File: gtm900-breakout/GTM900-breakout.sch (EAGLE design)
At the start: 43 parts, among them K1 694108106102, T1 BC847, U1 FH12A-40S-0.5SH(55), U2 FH12A-40S-0.5SH(55), U3 MCP1827T-ADJE/ET

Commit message: gtm900: added CP2105 and 3.5mm TRRS audio jack, remv'd aux conn
adds to OS#4030
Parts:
- removed JP2: (no value), jumper:JP1E
- added C15, C19: 4.7u, rc-sysmocom:CAP_CERAMIC_0603
- added C16: 1u, rc-sysmocom:CAP_CERAMIC_0603
- added C17, C18, C20, C27, C28: 100n, rc-sysmocom:CAP_CERAMIC_0603
- added C21, C22, C23, C24, C25, C26, C30, C31, C32: 33p, rc-sysmocom:CAP_CERAMIC_0402
- added C29: 22u, rc-sysmocom:CAP_CERAMIC_0603
- added J1: SJ2-3574A, SparkFun-Connectors:AUDIO-JACK3
- added K2: 615004143821, Wuerth_Elektronik_eiCan_Communication_Connectors_v6_20150113:615004143821
- added R12: 4.7k, rc-sysmocom:RESISTOR_0603
- added R13: 1M, rc-sysmocom:RESISTOR_0603
- added R14, R17: 100, rc-sysmocom:RESISTOR_0402
- added R15, R16: 2.2k, rc-sysmocom:RESISTOR_0402
- added U4: CP2105-GM, usb-uart:CP2105-GM
- added U5: IP4234CZ6, laforge:IP4234CZ6
- added X3: MINI-USB-SHIELD-UX60-MB-5ST, con-hirose:MINI-USB-SHIELD-UX60-MB-5ST
- B1, MDM1: CLASS (none) -> UNKNOWN CLASS; DESCRIPTION (none) -> NO DESCRIPTION; LINK (none) -> UNKNOWN LINK; MANUFACTURER (none) -> UNKNOWN MANUFACTURER; MANUFACTURERPARTNUMBER (none) -> UNKNOWN MANUFACTURER PART NUMBER; POPULATED (none) -> TRUE; ROHSCERTIFICATE (none) -> UNKNOWN ROHS CERTIFICATE; SOURCE (none) -> UNKNOWN SOURCE; SOURCEPARTNUMBER (none) -> UNKNOWN SOURCE PART NUMBER
- JP1: device laforge:PINHD-2X10 -> jumper:JP1E
- R11: value 22k -> 15k; DESCRIPTION RES 22K OHM 1/10W 1% 0603 SMD -> RES SMD 15K OHM 1%% 1/10W 0603; LINK http://www.digikey.de/product-detail/de/MCR03ERTF2202/RHM22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 -> https://www.digikey.de/product-detail/de/yageo/RC0603FR-071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; MANUFACTURER Rohm Semiconductor -> Yageo; MANUFACTURERPARTNUMBER MCR03ERTF2202 -> RC0603FR-0715KL; ROHSCERTIFICATE Bleifrei / RoHS-konform -> UNKNOWN ROHS CERTIFICATE; SOURCEPARTNUMBER RHM22.0KCFCT-ND -> 311-15.0KHRCT-ND
- R6: value 200k -> 22k; DESCRIPTION RES 200K OHM 1/16W 1% 0603 -> RES 22K OHM 1/10W 1% 0603 SMD; LINK http://www.digikey.de/product-detail/de/8-1879338-5/A102235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 -> http://www.digikey.de/product-detail/de/MCR03ERTF2202/RHM22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; MANUFACTURER TE Connectivity -> Rohm Semiconductor; MANUFACTURERPARTNUMBER 8-1879338-5 -> MCR03ERTF2202; SOURCEPARTNUMBER A102235CT-ND -> RHM22.0KCFCT-ND
- R8: value 15k -> 330; DESCRIPTION RES SMD 15K OHM 1%% 1/10W 0603 -> RES SMD 330 OHM 5% 1/10W 0603; LINK https://www.digikey.de/product-detail/de/yageo/RC0603FR-071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 -> http://www.digikey.com/product-detail/en/yageo/RC0603JR-073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; MANUFACTURERPARTNUMBER RC0603FR-0715KL -> RC0603JR-07330RL; SOURCEPARTNUMBER 311-15.0KHRCT-ND -> 311-330GRCT-ND
- R9: value 330 -> 200k; DESCRIPTION RES SMD 330 OHM 5% 1/10W 0603 -> RES 200K OHM 1/16W 1% 0603; LINK http://www.digikey.com/product-detail/en/yageo/RC0603JR-073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 -> http://www.digikey.de/product-detail/de/8-1879338-5/A102235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; MANUFACTURER Yageo -> TE Connectivity; MANUFACTURERPARTNUMBER RC0603JR-07330RL -> 8-1879338-5; ROHSCERTIFICATE UNKNOWN ROHS CERTIFICATE -> Bleifrei / RoHS-konform; SOURCEPARTNUMBER 311-330GRCT-ND -> A102235CT-ND
- U1, U2: CLASS (none) -> IC; DESCRIPTION (none) -> NO DESCRIPTION; LINK (none) -> UNKNOWN LINK; MANUFACTURER (none) -> UNKNOWN MANUFACTURER; MANUFACTURERPARTNUMBER (none) -> UNKNOWN MANUFACTURER PART NUMBER; POPULATED (none) -> TRUE; ROHSCERTIFICATE (none) -> UNKNOWN ROHS CERTIFICATE; SOURCE (none) -> UNKNOWN SOURCE; SOURCEPARTNUMBER (none) -> UNKNOWN SOURCE PART NUMBER
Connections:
- removed net N$24: JP1.12
- new net N$11: C20.2, R13.2, X3S.S1, X3S.S2, X3S.S3, X3S.S4
- new net N$12: R12.1, U4.!RST
- new net N$14: C15.2, U4.NC/DCD_ECI
- new net N$15: C27.2, C31.1, J1.RING2, R15.2
- new net N$16: C29.1, C30.1, R14.2, R15.1
- new net N$17: C29.2, C30.2, R16.2, R17.1
- new net N$20: C28.2, C31.2, J1.TIP, R16.1
- new net USB_DN: U4.D_MINUS, U5.2B
- new net USB_DP: U4.D_PLUS, U5.1B
- new net USB_VBUS: C16.1, U4.REGIN, U4.VBUS, U5.VCC, X3G$1.1
- new net VDD_3V45: C18.1, C19.1, U4.VDD
- new net _USB_DN: U5.2A, X3G$1.2
- new net _USB_DP: U5.1A, X3G$1.3
- net !RST: now also R11.2; no longer R8.2
- net ADC: no longer JP1.2
- net AUXI+: no longer JP1.19
- net AUXI-: no longer JP1.20
- net AUXO+: no longer JP1.13
- net AUXO-: no longer JP1.14
- net EAR+: now also C23.1, C26.1, C32.2, J1.RING1; no longer JP1.15
- net EAR-: now also C24.2, C26.2, C32.1, J1.EARTH; no longer JP1.16
- net GND: now also C15.1, C16.2, C17.1, C18.2, C19.2, C20.1, C21.2, C22.1, C23.2, C24.1, JP1.2, R13.1, R17.2, U4.GND, U4.HEAT_TAB, U5.GND, X3G$1.5; no longer JP1.3, JP2.2
- net LPG: now also R6.1; no longer R11.1
- net MIC+: now also C21.1, C25.1, C27.1; no longer JP1.17
- net MIC-: now also C22.2, C25.2, C28.1; no longer JP1.18
- net N$2: now also R8.2; no longer R9.2
- net N$5: now also R6.2, R7.1; no longer R10.1, R11.2
- net N$6: now also R10.1, R9.1; no longer R6.1, R7.1
- net PWON: now also JP1.1; no longer JP2.1
- net RXD2: now also U4.RXD_ECI
- net TXD2: now also U4.TXD_ECI
- net UART_CTS: now also U4.CTS_SCI; no longer JP1.8
- net UART_DCD: now also U4.GPIO.0_SCI/DCD_SCI; no longer JP1.11
- net UART_DSR: now also U4.GPIO.2_SCI/DSR_SCI; no longer JP1.4
- net UART_DTR: now also U4.GPIO.1_SCI/DTR_SCI; no longer JP1.10
- net UART_RI: now also U4.!SUSPEND/RI_SCI; no longer JP1.5
- net UART_RTS: now also U4.RTS_SCI; no longer JP1.9
- net UART_RXD: now also U4.RXD_SCI; no longer JP1.6
- net UART_TXD: now also U4.TXD_SCI; no longer JP1.7
- net VCC: now also R11.1, R9.2; no longer JP1.1, R6.2, R9.1
- net VDD: now also C17.2, R12.2, R14.1, U4.VIO
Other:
- note added: "audio i/o (1st channel)"
- note added: "dual USB UART"
- note added: "for programming"
- note removed: "AUX socket / I/O Header"

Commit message: gtm900-bo: hopefully incorporating all we discussed last weeks
see OS#4030
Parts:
- removed K2: 615004143821, Wuerth_Elektronik_eiCan_Communication_Connectors_v6_20150113:615004143821
- added B2: (no value), microbuilder:SWITCH_TACT_SMT
- added C33, C34: 33p, rc-sysmocom:CAP_CERAMIC_0402
- added D5: PESD5V0UBV, laforge:PESD5V0UBV
- added JP2: (no value), microbuilder:HEADER-1X476MIL
- added R18, R20, R21: 22k, rc-sysmocom:RESISTOR_0603
- added R19: 330, rc-sysmocom:RESISTOR_0603
- added R22: DNP, rc-sysmocom:RESISTOR_0603
- added R23: 1k, rc-sysmocom:RESISTOR_0603
- added R24: 4.7k, rc-sysmocom:RESISTOR_0603
- added R25: 1M, rc-sysmocom:RESISTOR_0603
- added R26: 0, rc-sysmocom:RESISTOR_0603
- added T2, T3, T4: BC847, transistor:BC847C-NPN-SOT23-BEC
- added TP1, TP2, TP3, TP4, TP5: TPTP10R, testpad:TPTP10R
- added U6: IP4234CZ6, laforge:IP4234CZ6
- added X4: MINI-USB-SHIELD-UX60-MB-5ST, con-hirose:MINI-USB-SHIELD-UX60-MB-5ST
- C10: value 470u -> 100u; device rcl:CPOL-EUUD-8X10 -> rc-sysmocom:CAP_CERAMIC1206; DESCRIPTION 470µF 6.3V Aluminum Capacitors Radial, Can - SMD 2000 Hrs @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 -> 100µF 6.3V Ceramic Capacitor X5R 1206 (3216 Metric) 0.126" 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; LINK http://www.digikey.com/product-detail/en/nichicon/UUR0J471M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 -> http://www.digikey.com/product-detail/en/murata-electronics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; MANUFACTURER Nichicon -> Murata Electronics North America; MANUFACTURERPARTNUMBER UUR0J471MNL1GS -> GRM31CR60J107ME39K; SOURCEPARTNUMBER 493-6207-1-ND -> 490-7217-1-ND
- C11: value 100u -> 470u; device rc-sysmocom:CAP_CERAMIC1206 -> rcl:CPOL-EUUD-8X10; DESCRIPTION 100µF 6.3V Ceramic Capacitor X5R 1206 (3216 Metric) 0.126" 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 -> 470µF 6.3V Aluminum Capacitors Radial, Can - SMD 2000 Hrs @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; LINK http://www.digikey.com/product-detail/en/murata-electronics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 -> http://www.digikey.com/product-detail/en/nichicon/UUR0J471M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; MANUFACTURER Murata Electronics North America -> Nichicon; MANUFACTURERPARTNUMBER GRM31CR60J107ME39K -> UUR0J471MNL1GS; SOURCEPARTNUMBER 490-7217-1-ND -> 493-6207-1-ND
- C13: value 10u -> 100n; device rc-sysmocom:CAP_CERAMIC_0805 -> rc-sysmocom:CAP_CERAMIC_0603; DESCRIPTION 10µF 16V Ceramic Capacitor X5R 0805 (2012 Metric) 0.079" L 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 -> CAP CER 0.1UF 16V 10% X7R 0603; LINK http://www.digikey.com/product-detail/en/samsung-electro-me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 -> http://www.digikey.com/product-detail/en/foo/1276-1005-1-ND; MANUFACTURER Samsung Electro-Mechanics America, Inc. -> Samsung Electro-Mechanics America, Inc; MANUFACTURERPARTNUMBER CL21A106KOQNNNG -> CL10B104KO8NNNC; ROHSCERTIFICATE UNKNOWN ROHS CERTIFICATE -> Bleifrei / RoHS-konform; SOURCEPARTNUMBER 1276-6455-1-ND -> 1276-1005-1-ND
- C14: value DNP -> 1u; device rcl:CPOL-EUSMCE -> rc-sysmocom:CAP_CERAMIC_0603; DESCRIPTION NO DESCRIPTION -> 1µF 16V Ceramic Capacitor X5R 0603 (1608 Metric) 0.063" L x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; LINK UNKNOWN LINK -> http://www.digikey.com/product-detail/en/murata-electronics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; MANUFACTURER UNKNOWN MANUFACTURER -> Murata Electronics North America; MANUFACTURERPARTNUMBER UNKNOWN MANUFACTURER PART NUMBER -> GRM188R61C105KA93J; POPULATED FALSE -> TRUE; SOURCE UNKNOWN SOURCE -> DIGIKEY; SOURCEPARTNUMBER UNKNOWN SOURCE PART NUMBER -> 490-6412-1-ND
- C15: value 4.7u -> 1u; DESCRIPTION 4.7µF 10V Ceramic Capacitor X5R 0603 (1608 Metric) 0.063" L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 -> 1µF 16V Ceramic Capacitor X5R 0603 (1608 Metric) 0.063" L x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; LINK http://www.digikey.com/product-detail/en/samsung-electro-me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 -> http://www.digikey.com/product-detail/en/murata-electronics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; MANUFACTURER Samsung Electro-Mechanics America, Inc. -> Murata Electronics North America; MANUFACTURERPARTNUMBER CL10A475KP8NNNC -> GRM188R61C105KA93J; SOURCEPARTNUMBER 1276-1044-1-ND -> 490-6412-1-ND
- C16: value 1u -> 10u; device rc-sysmocom:CAP_CERAMIC_0603 -> rc-sysmocom:CAP_CERAMIC_0805; DESCRIPTION 1µF 16V Ceramic Capacitor X5R 0603 (1608 Metric) 0.063" L x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 -> 10µF 16V Ceramic Capacitor X5R 0805 (2012 Metric) 0.079" L 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; LINK http://www.digikey.com/product-detail/en/murata-electronics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 -> http://www.digikey.com/product-detail/en/samsung-electro-me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; MANUFACTURER Murata Electronics North America -> Samsung Electro-Mechanics America, Inc.; MANUFACTURERPARTNUMBER GRM188R61C105KA93J -> CL21A106KOQNNNG; SOURCEPARTNUMBER 490-6412-1-ND -> 1276-6455-1-ND
- C17: value 100n -> DNP; device rc-sysmocom:CAP_CERAMIC_0603 -> rcl:CPOL-EUSMCE; DESCRIPTION 0.10µF 16V Ceramic Capacitor X5R 0201 (0603 Metric) 0.024" 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 -> NO DESCRIPTION; LINK http://www.digikey.com/product-detail/en/murata-electronics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 -> UNKNOWN LINK; MANUFACTURER Murata Electronics North America -> UNKNOWN MANUFACTURER; MANUFACTURERPARTNUMBER GRM033R61C104KE84D -> UNKNOWN MANUFACTURER PART NUMBER; POPULATED TRUE -> FALSE; SOURCE DIGIKEY -> UNKNOWN SOURCE; SOURCEPARTNUMBER 490-9985-1-ND -> UNKNOWN SOURCE PART NUMBER
- C18: DESCRIPTION 0.10µF 16V Ceramic Capacitor X5R 0201 (0603 Metric) 0.024" 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 -> CAP CER 0.1UF 16V 10% X7R 0603; LINK http://www.digikey.com/product-detail/en/murata-electronics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 -> http://www.digikey.com/product-detail/en/foo/1276-1005-1-ND; MANUFACTURER Murata Electronics North America -> Samsung Electro-Mechanics America, Inc; MANUFACTURERPARTNUMBER GRM033R61C104KE84D -> CL10B104KO8NNNC; ROHSCERTIFICATE UNKNOWN ROHS CERTIFICATE -> Bleifrei / RoHS-konform; SOURCEPARTNUMBER 490-9985-1-ND -> 1276-1005-1-ND
- C20: value 100n -> 1u; DESCRIPTION 0.10µF 16V Ceramic Capacitor X5R 0201 (0603 Metric) 0.024" 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 -> 1µF 16V Ceramic Capacitor X5R 0603 (1608 Metric) 0.063" L x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; LINK http://www.digikey.com/product-detail/en/murata-electronics-north-america/GRM033R61C104KE84D/490-9985-1-ND/5026290 -> http://www.digikey.com/product-detail/en/murata-electronics-north-america/GRM188R61C105KA93J/490-6412-1-ND/3845609; MANUFACTURERPARTNUMBER GRM033R61C104KE84D -> GRM188R61C105KA93J; SOURCEPARTNUMBER 490-9985-1-ND -> 490-6412-1-ND
- C21, C22, C24: value 33p -> 100n; device rc-sysmocom:CAP_CERAMIC_0402 -> rc-sysmocom:CAP_CERAMIC_0603; DESCRIPTION CAP CER 33PF 50V NP0 0402 -> 0.10µF 16V Ceramic Capacitor X5R 0201 (0603 Metric) 0.024" 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; LINK http://www.digikey.com/product-detail/en/CL05C330JB5NNNC/12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 -> http://www.digikey.com/product-detail/en/murata-electronics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; MANUFACTURER Samsung Electro-Mechanics America, Inc. -> Murata Electronics North America; MANUFACTURERPARTNUMBER CL05C330JB5NNNC -> GRM033R61C104KE84D; ROHSCERTIFICATE Bleifrei / RoHS-konform -> UNKNOWN ROHS CERTIFICATE; SOURCEPARTNUMBER 1276-1272-1-ND -> 490-9985-1-ND
- C23: value 33p -> 4.7u; device rc-sysmocom:CAP_CERAMIC_0402 -> rc-sysmocom:CAP_CERAMIC_0603; DESCRIPTION CAP CER 33PF 50V NP0 0402 -> 4.7µF 10V Ceramic Capacitor X5R 0603 (1608 Metric) 0.063" L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; LINK http://www.digikey.com/product-detail/en/CL05C330JB5NNNC/12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 -> http://www.digikey.com/product-detail/en/samsung-electro-me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; MANUFACTURERPARTNUMBER CL05C330JB5NNNC -> CL10A475KP8NNNC; ROHSCERTIFICATE Bleifrei / RoHS-konform -> UNKNOWN ROHS CERTIFICATE; SOURCEPARTNUMBER 1276-1272-1-ND -> 1276-1044-1-ND
- C27, C28: value 100n -> 33p; device rc-sysmocom:CAP_CERAMIC_0603 -> rc-sysmocom:CAP_CERAMIC_0402; DESCRIPTION CAP CER 0.1UF 16V 10% X7R 0603 -> CAP CER 33PF 50V NP0 0402; LINK http://www.digikey.com/product-detail/en/foo/1276-1005-1-ND -> http://www.digikey.com/product-detail/en/CL05C330JB5NNNC/12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; MANUFACTURER Samsung Electro-Mechanics America, Inc -> Samsung Electro-Mechanics America, Inc.; MANUFACTURERPARTNUMBER CL10B104KO8NNNC -> CL05C330JB5NNNC; SOURCEPARTNUMBER 1276-1005-1-ND -> 1276-1272-1-ND
- C29: value 22u -> 33p; device rc-sysmocom:CAP_CERAMIC_0603 -> rc-sysmocom:CAP_CERAMIC_0402; DESCRIPTION CAP CER 22UF 6.3V 20% X5R 0603 -> CAP CER 33PF 50V NP0 0402; LINK http://www.digikey.de/product-detail/de/foo/445-8028-1-ND -> http://www.digikey.com/product-detail/en/CL05C330JB5NNNC/12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; MANUFACTURER TDK Corporation -> Samsung Electro-Mechanics America, Inc.; MANUFACTURERPARTNUMBER C1608X5R0J226M080AC -> CL05C330JB5NNNC; SOURCEPARTNUMBER 445-8028-1-ND -> 1276-1272-1-ND
- C31, C32: value 33p -> 10u; device rc-sysmocom:CAP_CERAMIC_0402 -> rc-sysmocom:CAP_CERAMIC_0805; DESCRIPTION CAP CER 33PF 50V NP0 0402 -> 10µF 16V Ceramic Capacitor X5R 0805 (2012 Metric) 0.079" L 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; LINK http://www.digikey.com/product-detail/en/CL05C330JB5NNNC/12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 -> http://www.digikey.com/product-detail/en/samsung-electro-me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; MANUFACTURERPARTNUMBER CL05C330JB5NNNC -> CL21A106KOQNNNG; ROHSCERTIFICATE Bleifrei / RoHS-konform -> UNKNOWN ROHS CERTIFICATE; SOURCEPARTNUMBER 1276-1272-1-ND -> 1276-6455-1-ND
- J1: value SJ2-3574A -> AUDIO-JACK3; CLASS CONNECTOR\JUMPER -> (none); DESCRIPTION NO DESCRIPTION -> (none); LINK https://www.digikey.de/product-detail/de/cui-devices/SJ2-35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 -> (none); MANUFACTURER UNKNOWN MANUFACTURER -> (none); MANUFACTURERPARTNUMBER UNKNOWN MANUFACTURER PART NUMBER -> (none); POPULATED TRUE -> (none); ROHSCERTIFICATE UNKNOWN ROHS CERTIFICATE -> (none); SOURCE UNKNOWN SOURCE -> (none); SOURCEPARTNUMBER UNKNOWN SOURCE PART NUMBER -> (none)
- MDM1: value GTM900-B -> GTM900-BM2-SPACER; device GTM900:GTM900-B -> GTM900:GTM900-BM2-SPACER
- R1: value 47 -> 15k; DESCRIPTION RES SMD 47 OHM 5% 1/10W 0603 -> RES SMD 15K OHM 1%% 1/10W 0603; LINK http://www.digikey.com/product-detail/en/yageo/RC0603JR-074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 -> https://www.digikey.de/product-detail/de/yageo/RC0603FR-071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; MANUFACTURERPARTNUMBER RC0603JR-0747RL -> RC0603FR-0715KL; SOURCEPARTNUMBER 311-47GRCT-ND -> 311-15.0KHRCT-ND
- R11: value 15k -> 4.7k; DESCRIPTION RES SMD 15K OHM 1%% 1/10W 0603 -> RES SMD 4.7K OHM 5% 1/10W 0603; LINK https://www.digikey.de/product-detail/de/yageo/RC0603FR-071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 -> http://www.digikey.com/product-detail/en/yageo/RC0603JR-074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; MANUFACTURERPARTNUMBER RC0603FR-0715KL -> RC0603JR-074K7L; SOURCEPARTNUMBER 311-15.0KHRCT-ND -> 311-4.7KGRCT-ND
- R12: value 4.7k -> DNP; DESCRIPTION RES SMD 4.7K OHM 5% 1/10W 0603 -> RES SMD 15K OHM 1%% 1/10W 0603; LINK http://www.digikey.com/product-detail/en/yageo/RC0603JR-074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 -> https://www.digikey.de/product-detail/de/yageo/RC0603FR-071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; MANUFACTURERPARTNUMBER RC0603JR-074K7L -> RC0603FR-0715KL; SOURCEPARTNUMBER 311-4.7KGRCT-ND -> 311-15.0KHRCT-ND
- R13: value 1M -> 1k; DESCRIPTION RES SMD 1M OHM 5% 1/20W 0201 -> NO DESCRIPTION; LINK http://www.digikey.com/product-detail/en/samsung-electro-me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 -> UNKNOWN LINK; MANUFACTURER Samsung Electro-Mechanics America, Inc. -> UNKNOWN MANUFACTURER; MANUFACTURERPARTNUMBER RC0603J105CS -> UNKNOWN MANUFACTURER PART NUMBER; SOURCE DIGIKEY -> UNKNOWN SOURCE; SOURCEPARTNUMBER 1276-3856-1-ND -> UNKNOWN SOURCE PART NUMBER
- R14: value 100 -> 0; device rc-sysmocom:RESISTOR_0402 -> rc-sysmocom:RESISTOR_0603; LINK http://www.digikey.de/product-detail/de/RC0603JR-07100RL/31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 -> http://www.digikey.de/product-detail/de/AC0402JR-070RL/311-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
- R15: value 2.2k -> 200k; device rc-sysmocom:RESISTOR_0402 -> rc-sysmocom:RESISTOR_0603; DESCRIPTION RES 2.20K OHM 1/16W 1% 0402 SMD -> RES 200K OHM 1/16W 1% 0603; LINK http://www.digikey.de/product-detail/de/RC0402FR-072K2L/311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 -> http://www.digikey.de/product-detail/de/8-1879338-5/A102235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; MANUFACTURER Yageo -> TE Connectivity; MANUFACTURERPARTNUMBER RC0402FR-072K2L -> 8-1879338-5; SOURCEPARTNUMBER 311-2.20KLRCT-ND -> A102235CT-ND
- R16: value 2.2k -> 22k; device rc-sysmocom:RESISTOR_0402 -> rc-sysmocom:RESISTOR_0603; DESCRIPTION RES 2.20K OHM 1/16W 1% 0402 SMD -> RES 22K OHM 1/10W 1% 0603 SMD; LINK http://www.digikey.de/product-detail/de/RC0402FR-072K2L/311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 -> http://www.digikey.de/product-detail/de/MCR03ERTF2202/RHM22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; MANUFACTURER Yageo -> Rohm Semiconductor; MANUFACTURERPARTNUMBER RC0402FR-072K2L -> MCR03ERTF2202; SOURCEPARTNUMBER 311-2.20KLRCT-ND -> RHM22.0KCFCT-ND
- R17: value 100 -> 22k; device rc-sysmocom:RESISTOR_0402 -> rc-sysmocom:RESISTOR_0603; DESCRIPTION NO DESCRIPTION -> RES 22K OHM 1/10W 1% 0603 SMD; LINK http://www.digikey.de/product-detail/de/RC0603JR-07100RL/31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 -> http://www.digikey.de/product-detail/de/MCR03ERTF2202/RHM22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; MANUFACTURER UNKNOWN MANUFACTURER -> Rohm Semiconductor; MANUFACTURERPARTNUMBER UNKNOWN MANUFACTURER PART NUMBER -> MCR03ERTF2202; ROHSCERTIFICATE UNKNOWN ROHS CERTIFICATE -> Bleifrei / RoHS-konform; SOURCE UNKNOWN SOURCE -> DIGIKEY; SOURCEPARTNUMBER UNKNOWN SOURCE PART NUMBER -> RHM22.0KCFCT-ND
- R3: value 15k -> 47; DESCRIPTION RES SMD 15K OHM 1%% 1/10W 0603 -> RES SMD 47 OHM 5% 1/10W 0603; LINK https://www.digikey.de/product-detail/de/yageo/RC0603FR-071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 -> http://www.digikey.com/product-detail/en/yageo/RC0603JR-074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; MANUFACTURERPARTNUMBER RC0603FR-0715KL -> RC0603JR-0747RL; SOURCEPARTNUMBER 311-15.0KHRCT-ND -> 311-47GRCT-ND
- R4: value 47 -> 4.7k; DESCRIPTION RES SMD 47 OHM 5% 1/10W 0603 -> RES SMD 4.7K OHM 5% 1/10W 0603; LINK http://www.digikey.com/product-detail/en/yageo/RC0603JR-0747RL/311-47GRCT-ND/729740 -> http://www.digikey.com/product-detail/en/yageo/RC0603JR-074K7L/311-4.7KGRCT-ND/729732; MANUFACTURERPARTNUMBER RC0603JR-0747RL -> RC0603JR-074K7L; SOURCEPARTNUMBER 311-47GRCT-ND -> 311-4.7KGRCT-ND
- R5: value 330 -> 47k; DESCRIPTION RES SMD 330 OHM 5% 1/10W 0603 -> NO DESCRIPTION; LINK http://www.digikey.com/product-detail/en/yageo/RC0603JR-073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 -> https://www.digikey.de/product-detail/de/stackpole-electron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; MANUFACTURER Yageo -> UNKNOWN MANUFACTURER; MANUFACTURERPARTNUMBER RC0603JR-07330RL -> UNKNOWN MANUFACTURER PART NUMBER; SOURCE DIGIKEY -> UNKNOWN SOURCE; SOURCEPARTNUMBER 311-330GRCT-ND -> UNKNOWN SOURCE PART NUMBER
- R6: value 22k -> 330; DESCRIPTION RES 22K OHM 1/10W 1% 0603 SMD -> RES SMD 330 OHM 5% 1/10W 0603; LINK http://www.digikey.de/product-detail/de/MCR03ERTF2202/RHM22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 -> http://www.digikey.com/product-detail/en/yageo/RC0603JR-073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; MANUFACTURER Rohm Semiconductor -> Yageo; MANUFACTURERPARTNUMBER MCR03ERTF2202 -> RC0603JR-07330RL; ROHSCERTIFICATE Bleifrei / RoHS-konform -> UNKNOWN ROHS CERTIFICATE; SOURCEPARTNUMBER RHM22.0KCFCT-ND -> 311-330GRCT-ND
- R8: value 330 -> 22k; DESCRIPTION RES SMD 330 OHM 5% 1/10W 0603 -> RES 22K OHM 1/10W 1% 0603 SMD; LINK http://www.digikey.com/product-detail/en/yageo/RC0603JR-073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 -> http://www.digikey.de/product-detail/de/MCR03ERTF2202/RHM22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; MANUFACTURER Yageo -> Rohm Semiconductor; MANUFACTURERPARTNUMBER RC0603JR-07330RL -> MCR03ERTF2202; ROHSCERTIFICATE UNKNOWN ROHS CERTIFICATE -> Bleifrei / RoHS-konform; SOURCEPARTNUMBER 311-330GRCT-ND -> RHM22.0KCFCT-ND
- R9: value 200k -> 22k; DESCRIPTION RES 200K OHM 1/16W 1% 0603 -> RES 22K OHM 1/10W 1% 0603 SMD; LINK http://www.digikey.de/product-detail/de/8-1879338-5/A102235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 -> http://www.digikey.de/product-detail/de/MCR03ERTF2202/RHM22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; MANUFACTURER TE Connectivity -> Rohm Semiconductor; MANUFACTURERPARTNUMBER 8-1879338-5 -> MCR03ERTF2202; SOURCEPARTNUMBER A102235CT-ND -> RHM22.0KCFCT-ND
- U4: value CP2105-GM -> MIC5366; device usb-uart:CP2105-GM -> ldo:LDO_FIXED_EN-MIC5365-YC5; DESCRIPTION USB Bridge, USB to UART USB 2.0 UART Interface 24-QFN (4x4) -> NO DESCRIPTION; LINK http://www.digikey.com/product-detail/en/silicon-labs/CP210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 -> https://www.digikey.de/product-detail/de/microchip-technolo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; MANUFACTURER Silicon Labs -> UNKNOWN MANUFACTURER; MANUFACTURERPARTNUMBER CP2105-F01-GM -> UNKNOWN MANUFACTURER PART NUMBER; SOURCE DIGIKEY -> UNKNOWN SOURCE; SOURCEPARTNUMBER 336-2009-5-ND -> UNKNOWN SOURCE PART NUMBER
- U5: value IP4234CZ6 -> CP2105-GM; device laforge:IP4234CZ6 -> usb-uart:CP2105-GM; DESCRIPTION TVS DIODE 5.5VWM 6TSOP -> USB Bridge, USB to UART USB 2.0 UART Interface 24-QFN (4x4); LINK http://www.digikey.com/product-detail/en/nxp-semiconductors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 -> http://www.digikey.com/product-detail/en/silicon-labs/CP210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; MANUFACTURER NXP Semiconductors -> Silicon Labs; MANUFACTURERPARTNUMBER IP4234CZ6,125 -> CP2105-F01-GM; SOURCEPARTNUMBER 568-5869-1-ND -> 336-2009-5-ND
- X1: device laforge:SMA-F-S-TH -> laforge:PINHD-1X3PTH; CLASS CONNECTOR -> (none); DESCRIPTION CONN SMA JACK STR 50 OHM PCB -> (none); LINK http://www.digikey.com/product-detail/en/te-connectivity-am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 -> (none); MANUFACTURER TE Connectivity AMP Connectors -> (none); MANUFACTURERPARTNUMBER 5-1814832-1 -> (none); POPULATED TRUE -> (none); ROHSCERTIFICATE UNKNOWN ROHS CERTIFICATE -> (none); SOURCE DIGIKEY -> (none); SOURCEPARTNUMBER A97594-ND -> (none)
- X2: device laforge:HRS_UFL -> laforge:SMA-F-S-TH; CLASS UNKNOWN CLASS -> CONNECTOR; DESCRIPTION CONN UMC RCPT STR 50 OHM SMD -> CONN SMA JACK STR 50 OHM PCB; LINK http://www.digikey.com/product-detail/en/hirose-electric-co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 -> http://www.digikey.com/product-detail/en/te-connectivity-am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; MANUFACTURER Hirose Electric Co Ltd -> TE Connectivity AMP Connectors; MANUFACTURERPARTNUMBER U.FL-R-SMT(01) -> 5-1814832-1; SOURCEPARTNUMBER H9161-ND -> A97594-ND
- X3: value MINI-USB-SHIELD-UX60-MB-5ST -> (none); device con-hirose:MINI-USB-SHIELD-UX60-MB-5ST -> laforge:HRS_UFL; CLASS CONNECTOR -> UNKNOWN CLASS; DESCRIPTION USB - mini B USB 2.0 Receptacle Connector 5 Position Surfac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 -> CONN UMC RCPT STR 50 OHM SMD; LINK http://www.digikey.com/product-detail/en/hirose-electric-co-ltd/UX60-MB-5ST/H2959CT-ND/597538 -> http://www.digikey.com/product-detail/en/hirose-electric-co-ltd/U.FL-R-SMT(01)/H9161-ND/513010; MANUFACTURERPARTNUMBER UX60-MB-5ST -> U.FL-R-SMT(01); SOURCEPARTNUMBER H2959CT-ND -> H9161-ND
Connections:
- removed net N$20: C28.2, C31.2, J1.TIP, R16.1
- removed net PWON: JP1.1, U1.26, U2.15
- removed net USB_DN: U4.D_MINUS, U5.2B
- removed net USB_DP: U4.D_PLUS, U5.1B
- removed net _USIM_IO: R4.1, U1.15, U2.26
- new net !PWON: C18.1, JP1.1, R22.2, R23.1, T4.C, U1.26, U2.15
- new net GPIO.0_ECI/DTR_ECI: R14.2, R20.1, U5.GPIO.0_ECI/DTR_ECI
- new net GPIO.1_ECI/DSR_ECI: R7.1, U5.GPIO.1_ECI/DSR_ECI
- new net N$10: R4.1, SIM1-DETECT.1@A
- new net N$18: R11.1, R14.1, T2.C
- new net N$21: B1.P, B1.P1, R13.2
- new net N$7: R10.1, R8.2, T2.B
- new net N$8: C32.1, C34.2, J1.RING1, J1.TIP
- new net N$9: B2.P, B2.P1, R23.2
- new net USB_D_N: U5.D_MINUS, U6.2B
- new net USB_D_P: U5.D_PLUS, U6.1B
- new net VIO_2V8: C15.2, C21.2, R11.2, R12.1, R22.1, U4.OUT, U5.VIO
- net !RST: now also C13.1, R12.2, R13.1, T1.C; no longer B1.P, B1.P1, R11.2
- net ADC: now also X1.1
- net AUXI+: now also TP3.TP
- net AUXI-: now also TP5.TP
- net AUXO+: now also TP2.TP
- net AUXO-: now also TP4.TP
- net EAR+: now also C25.2, D5.3, JP2.3; no longer C23.1, J1.RING1
- net EAR-: now also C25.1, C27.2, D5.1, JP2.4, R26.2; no longer C24.2, C26.2, C32.1, J1.EARTH
- net GND: now also B2.S, B2.S1, C10.1, C11.-, C13.2, C14.1, C16.1, C17.-, C19.1, C20.2, C21.1, C22.2, C26.2, C27.1, C28.2, C29.2, C31.2, C33.2, C34.1, D5.GND, J1.RING2, R16.2, R18.2, R21.2, R25.1, R26.1, R6.1, R9.2, T2.E, T3.E, T4.E, U5.HEAT_TAB, U6.GND, X1.3, X2.GND@3, X2.GND@4, X3.GND@1, X3.GND@2, X4G$1.5; no longer C10.-, C11.1, C13.1, C14.-, C16.2, C17.1, C19.2, C20.1, C21.2, C22.1, R13.1, R17.2, R7.2, U4.HEAT_TAB, X1.GND@1, X1.GND@2, X1.GND@3, X1.GND@4, X3G$1.5
- net LDO_IN: now also C11.+; no longer C10.+
- net LPG: now also R17.1; no longer R6.1
- net MIC+: now also C28.1, C30.1, C33.1, D5.4, J1.EARTH, JP2.1; no longer C21.1, C25.1, C27.1
- net MIC-: now also C29.1, C30.2, C31.1, D5.5, JP2.2; no longer C22.2, C25.2, C28.1
- net N$1: now also R6.2; no longer R5.2
- net N$11: now also C24.2, R25.2, X4S.S1, X4S.S2, X4S.S3, X4S.S4; no longer C20.2, R13.2, X3S.S1, X3S.S2, X3S.S3, X3S.S4
- net N$12: now also R24.1, U5.!RST; no longer R12.1, U4.!RST
- net N$13: now also X3.1; no longer X1.1
- net N$14: now also C19.2, U5.NC/DCD_ECI; no longer C15.2, U4.NC/DCD_ECI
- net N$15: now also R4.2; no longer C27.2, C31.1, J1.RING2, R15.2
- net N$16: now also R20.2, R21.1, T4.B; no longer C29.1, C30.1, R14.2, R15.1
- net N$17: now also R7.2, R9.1, T1.B; no longer C29.2, C30.2, R16.2, R17.1
- net N$2: now also R19.2; no longer R8.2
- net N$3: now also T3.C; no longer T1.C
- net N$5: now also R17.2, R18.1, T3.B; no longer R6.2, R7.1, T1.B
- net N$6: now also R15.1, R16.1; no longer R10.1, R9.1
- net RXD2: now also U5.RXD_ECI; no longer U4.RXD_ECI
- net TXD2: now also U5.TXD_ECI; no longer U4.TXD_ECI
- net UART_CTS: now also U5.CTS_SCI; no longer U4.CTS_SCI
- net UART_DCD: now also U5.GPIO.0_SCI/DCD_SCI; no longer U4.GPIO.0_SCI/DCD_SCI
- net UART_DSR: now also U5.GPIO.2_SCI/DSR_SCI; no longer U4.GPIO.2_SCI/DSR_SCI
- net UART_DTR: now also R8.1, U5.GPIO.1_SCI/DTR_SCI; no longer U4.GPIO.1_SCI/DTR_SCI
- net UART_RI: now also U5.!SUSPEND/RI_SCI; no longer U4.!SUSPEND/RI_SCI
- net UART_RTS: now also U5.RTS_SCI; no longer U4.RTS_SCI
- net UART_RXD: now also U5.RXD_SCI; no longer U4.RXD_SCI
- net UART_TXD: now also U5.TXD_SCI; no longer U4.TXD_SCI
- net USB_VBUS: now also C14.2, C20.1, U4.EN, U4.IN, U5.REGIN, U5.VBUS, U6.VCC, X4G$1.1; no longer C16.1, U4.REGIN, U4.VBUS, U5.VCC, X3G$1.1
- net USIM_CD: now also R5.2, SIM1-DETECT.0@A
- net USIM_CLK: now also R3.2; no longer R2.2
- net USIM_IO: now also R1.1, U1.15, U2.26; no longer R3.1, R4.2
- net USIM_RESET: now also R2.2; no longer R1.2
- net USIM_VCC: now also R1.2; no longer R3.2
- net VBACKUP: now also X1.2
- net VCC: now also C10.2, C16.2, C17.+, R15.2, R19.1; no longer C11.2, C13.2, C14.+, R11.1, R8.1, R9.2
- net VDD: now also R24.2; no longer C17.2, R12.2, R14.1, U4.VIO
- net VDD_3V45: now also C22.1, C23.1, TP1.TP, U5.VDD; no longer C18.1, C19.1, U4.VDD
- net _USB_DN: now also U6.2A, X4G$1.2; no longer U5.2A, X3G$1.2
- net _USB_DP: now also U6.1A, X4G$1.3; no longer U5.1A, X3G$1.3
- net _USIM_CLK: now also R3.1; no longer R2.1
- net _USIM_RESET: now also R2.1; no longer R1.1
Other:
- note added: "power-on via DTR"
- note added: "power-on via GPIO.0_ECI/DTR_ECI"
- note removed: "power-on"
- moved on the sheet: B1, C1, C13, C19, C2, C20, C21, C22, C23, C24, C25, C26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

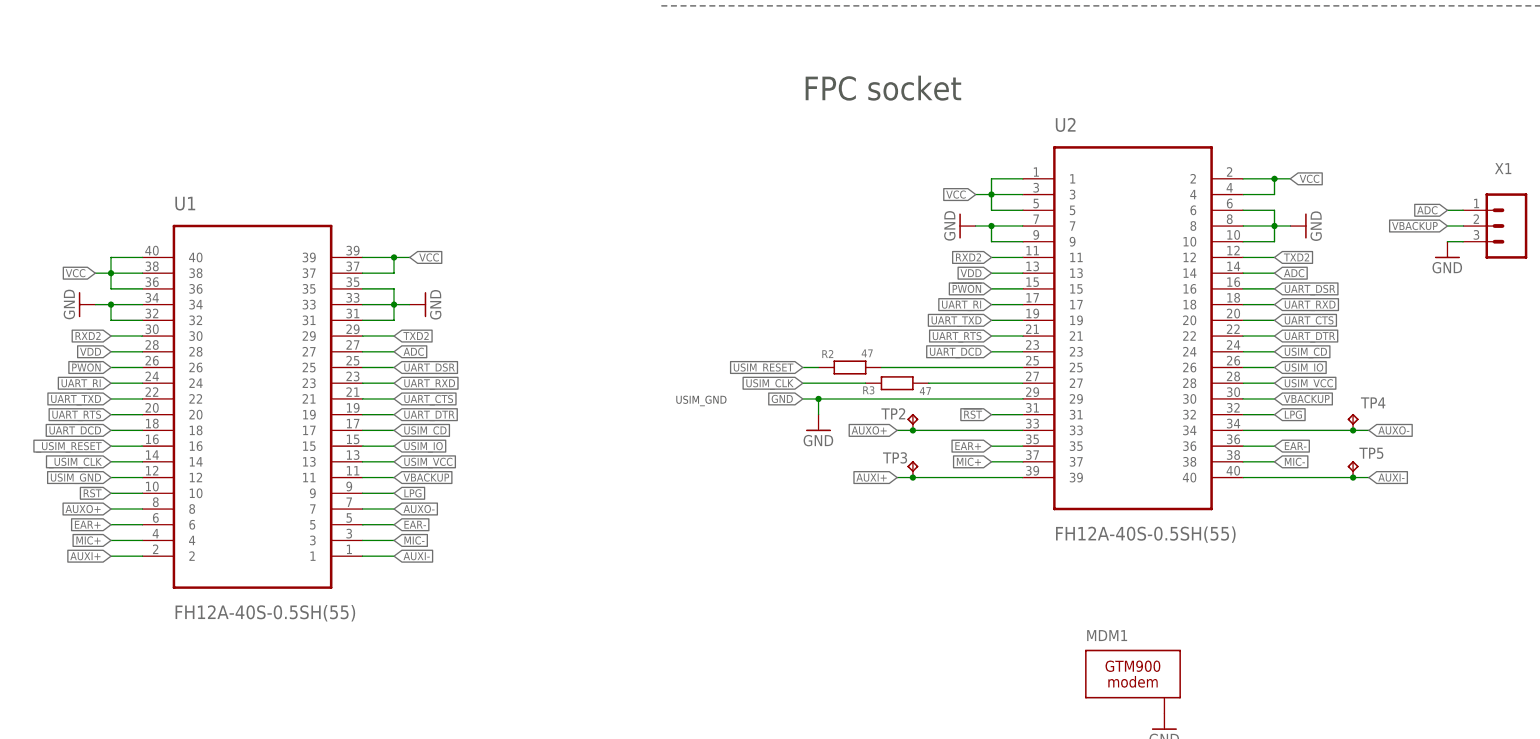
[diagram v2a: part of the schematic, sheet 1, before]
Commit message: gtm900-bo: routing done, no airwires left, mirrored FPC removed
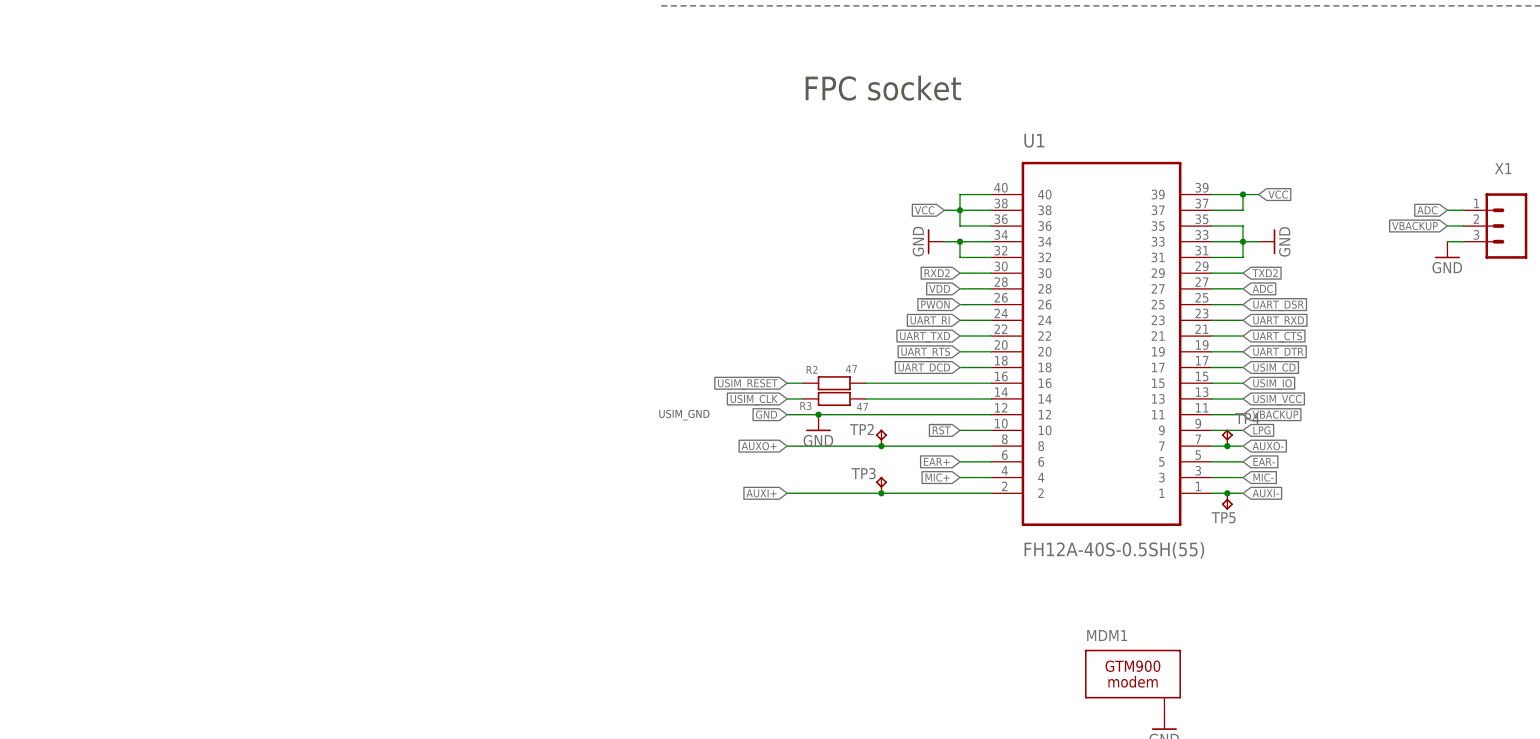
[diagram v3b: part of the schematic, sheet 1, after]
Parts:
- removed U2: FH12A-40S-0.5SH(55), FH12A-40S-0.5SH(55):FH12A-40S-0.5SH(55)
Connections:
- removed net USIM_GND: U1.12
- net !PWON: no longer U2.15
- net !RST: no longer U2.31
- net ADC: no longer U2.14
- net AUXI+: no longer U2.39
- net AUXI-: no longer U2.40
- net AUXO+: no longer U2.33
- net AUXO-: no longer U2.34
- net EAR+: no longer U2.35
- net EAR-: no longer U2.36
- net GND: now also U1.12; no longer U2.10, U2.29, U2.6, U2.7, U2.8, U2.9
- net LPG: no longer U2.32
- net MIC+: no longer U2.37
- net MIC-: no longer U2.38
- net RXD2: no longer U2.11
- net TXD2: no longer U2.12
- net UART_CTS: no longer U2.20
- net UART_DCD: no longer U2.23
- net UART_DSR: no longer U2.16
- net UART_DTR: no longer U2.22
- net UART_RI: no longer U2.17
- net UART_RTS: no longer U2.21
- net UART_RXD: no longer U2.18
- net UART_TXD: no longer U2.19
- net USIM_CD: no longer U2.24
- net USIM_IO: no longer U2.26
- net USIM_VCC: no longer U2.28
- net VBACKUP: no longer U2.30
- net VCC: no longer U2.1, U2.2, U2.3, U2.4, U2.5
- net VDD: no longer U2.13
- net _USIM_CLK: no longer U2.27
- net _USIM_RESET: no longer U2.25
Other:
- moved on the sheet: R2, R3, TP2, TP3, TP4, TP5, U1
